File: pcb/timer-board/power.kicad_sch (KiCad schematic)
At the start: 0 parts

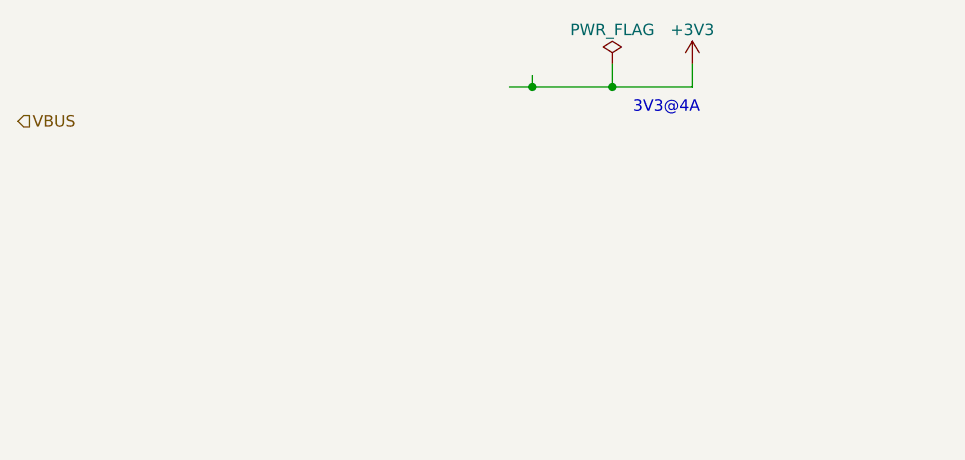
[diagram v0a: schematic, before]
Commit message: Connect OLED display, position main components
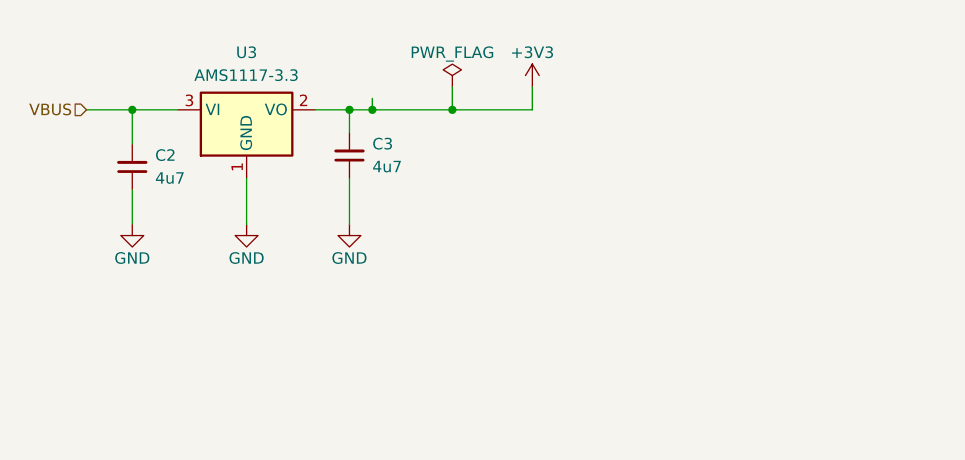
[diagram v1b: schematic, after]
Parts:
- added C2, C3: C-4u7-0402, DW-footprints:C_0402_1005Metric, symbol DW-capacitors:C-4u7-0402
- added U3: AMS1117-3.3, Package_TO_SOT_SMD:SOT-223-3_TabPin2, symbol Regulator_Linear:AMS1117-3.3
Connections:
- net +3V3: now also C3.2, U3.2 (VO)
- net VBUS: now also C2.2, U3.3 (VI)
- new net GND: C2.1, C3.1, U3.1 (GND)
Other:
- note removed: "3V3@4A"

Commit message: Finish uncompleted schematic sections, layout most of the PCB
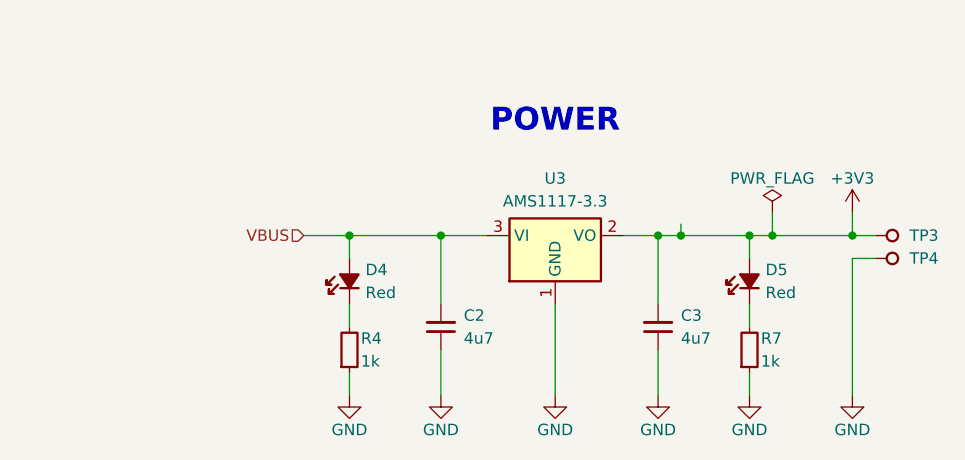
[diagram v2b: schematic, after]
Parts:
- added D4, D5: LED-R-0603_KT-0603R, DW-footprints:LED_0603_1608Metric_R, symbol DW-diodes:LED-R-0603_KT-0603R
- added R4, R7: R-1k-0402, DW-footprints:R_0402_1005Metric, symbol DW-resistors:R-1k-0402
- added TP3, TP4: TP_SMD_1mm, DW-footprints:TP_SMD_1mm, symbol DW-test-points:TP_SMD_1mm
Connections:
- net +3V3: now also D5.2 (A), TP3.1
- net GND: now also R4.1, R7.1, TP4.1
- net VBUS: now also D4.2 (A)
- new net: D4.1 (C), R4.2
- new net: D5.1 (C), R7.2
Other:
- note added: "POWER"
- moved on the sheet: C2, C3, U3

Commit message: Add I2C pull-up, IR receiver decoupling, LED labels, clear ERC and DRC
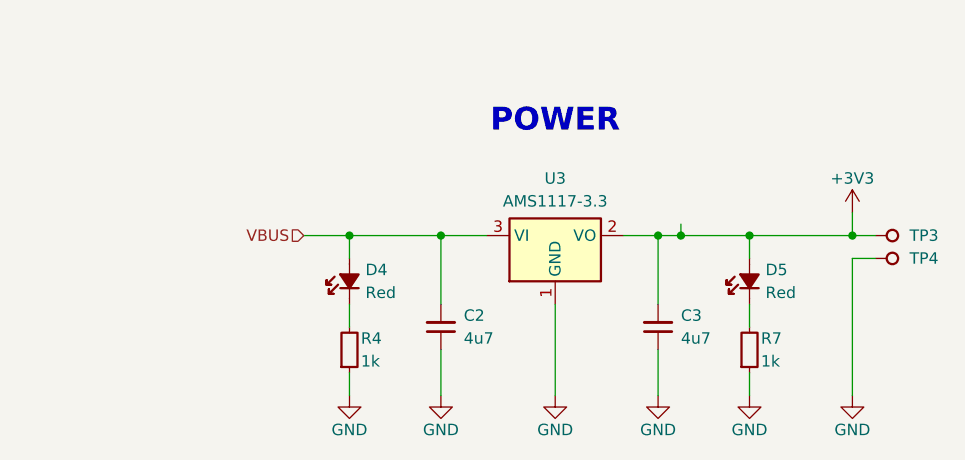
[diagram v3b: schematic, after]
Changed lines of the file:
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@@
-	)
-	(junction
-		(at 167.64 97.79)
-		(diameter 0)
-		(color 0 0 0 0)
 	)
 	(junction
@@
 	(wire
 		(pts
-			(xy 167.64 95.25) (xy 167.64 97.79)
-		)
-		(stroke
-			(width 0)
-			(type default)
-		)
-	)
-	(wire
-		(pts
 			(xy 165.1 97.79) (xy 165.1 100.33)
 		)
@@
 	(wire
 		(pts
-			(xy 165.1 97.79) (xy 167.64 97.79)
+			(xy 165.1 97.79) (xy 176.53 97.79)
 		)
 		(stroke
@@
 		(pts
 			(xy 120.65 113.03) (xy 120.65 115.57)
-		)
-		(stroke
-			(width 0)
-			(type default)
-		)
-	)
-	(wire
-		(pts
-			(xy 167.64 97.79) (xy 176.53 97.79)
 		)
 		(stroke
@@
 					(unit 1)
 				)
-			)
-		)
-	)
-	(symbol
-		(lib_id "DW-power-symbols:PWR_FLAG")
-		(at 167.64 95.25 0)
-		(unit 1)
-		(exclude_from_sim no)
-		(in_bom yes)
-		(on_board yes)
-		(dnp no)
-		(property "Reference" "#FLG06"
-			(at 167.64 93.345 0)
-			(effects
-				(font
-					(size 1.27 1.27)
-				)
-				(hide yes)
-			)
-		)
-		(property "Value" "PWR_FLAG"
-			(at 167.64 91.44 0)
-			(effects
-				(font
-					(size 1.27 1.27)
-				)
-			)
-		)
-		(property "Footprint" ""
-			(at 167.64 95.25 0)
-			(effects
-				(font
-					(size 1.27 1.27)
-				)
-				(hide yes)
-			)
-		)
-		(property "Datasheet" "~"
-			(at 167.64 95.25 0)
-			(effects
-				(font
-					(size 1.27 1.27)
-				)
-				(hide yes)
-			)
-		)
-		(property "Description" "Special symbol for telling ERC where power comes from"
-			(at 167.64 95.25 0)
-			(effects
-				(font
-					(size 1.27 1.27)
-				)
-				(hide yes)
-			)
-		)
-		(pin "1"
-		)
-		(instances
-			(project "timer-board"
-				(path "/c6951331-127b-46f8-97b9-b4f2222f059c/77f6e689-c08e-49eb-9519-227052faa756"
-					(reference "#FLG06")
-					(unit 1)
-				)
